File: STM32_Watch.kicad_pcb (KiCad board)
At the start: 2 copper layers, 40 x 45 mm, 44 parts, among them SW1 SW_Push, SW2 SW_Push, U1 STM32L031K6Ux, U3 LSM6DS3, X1 32.768k

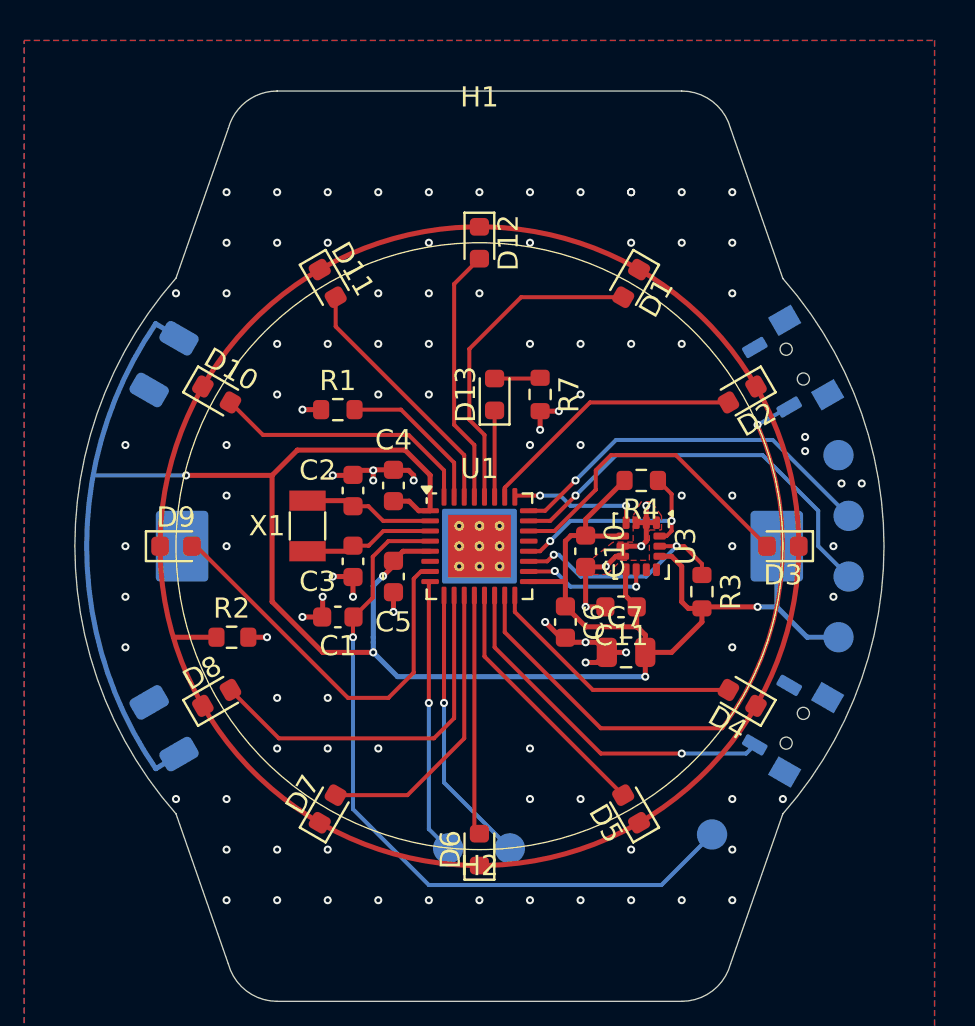
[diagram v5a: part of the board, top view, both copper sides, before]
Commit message: Updated Routing & Fixed DRC problems
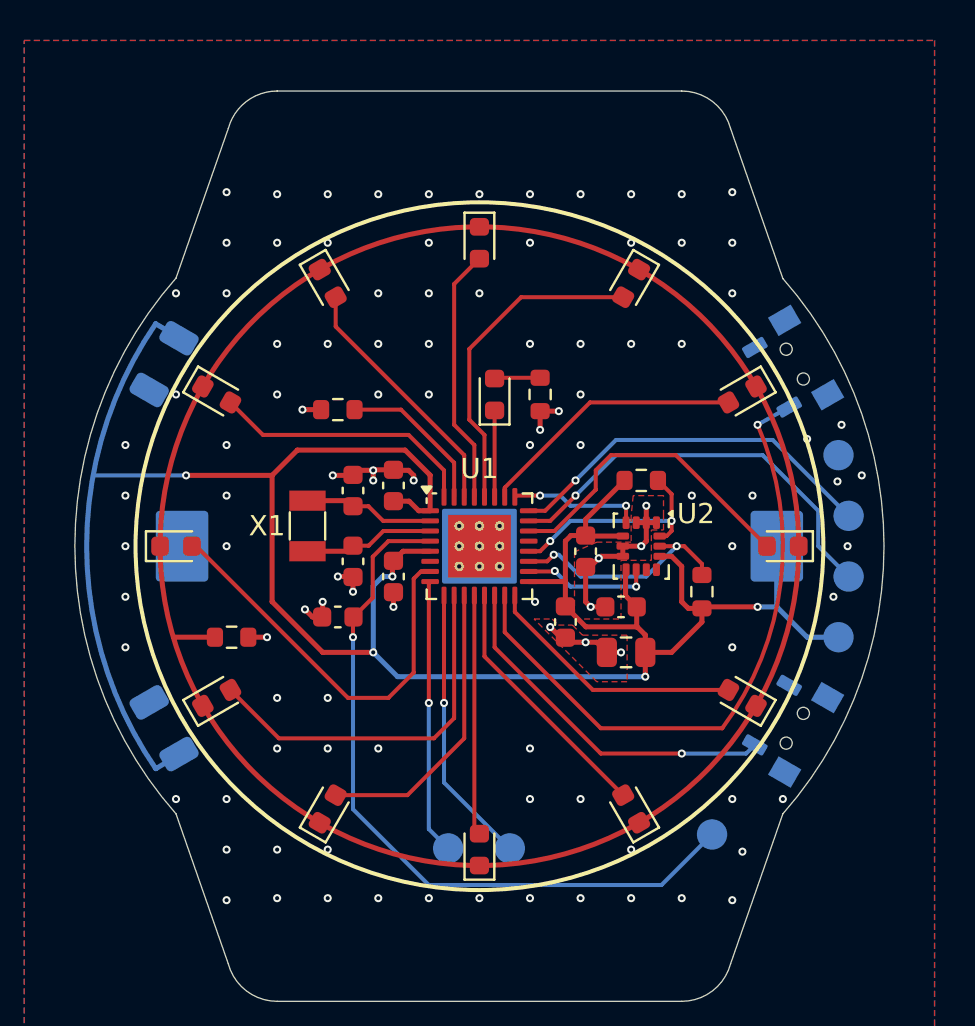
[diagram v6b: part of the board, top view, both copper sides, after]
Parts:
- removed R7: 1M, Resistor_SMD:R_0603_1608Metric
- removed U3: LSM6DS3, Package_LGA:LGA-14_3x2.5mm_P0.5mm_LayoutBorder3x4y
- added R5: 1M, Resistor_SMD:R_0603_1608Metric, F.Cu at (103.0, 92.5)
- added U2: LSM6DS3, Package_LGA:LGA-14_3x2.5mm_P0.5mm_LayoutBorder3x4y, F.Cu at (108.0, 100.0)
- turned TP5 to -90 degrees
- turned TP6 to -90 degrees
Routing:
- net GND: track 29.3 -> 26.3 mm, vias 106 -> 107
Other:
- board text added: "3V3"
- board text added: "CL"
- board text added: "GND"
- board text added: "IO"
- board text added: "NRST"
- board text added: "RX"
- board text added: "TX"

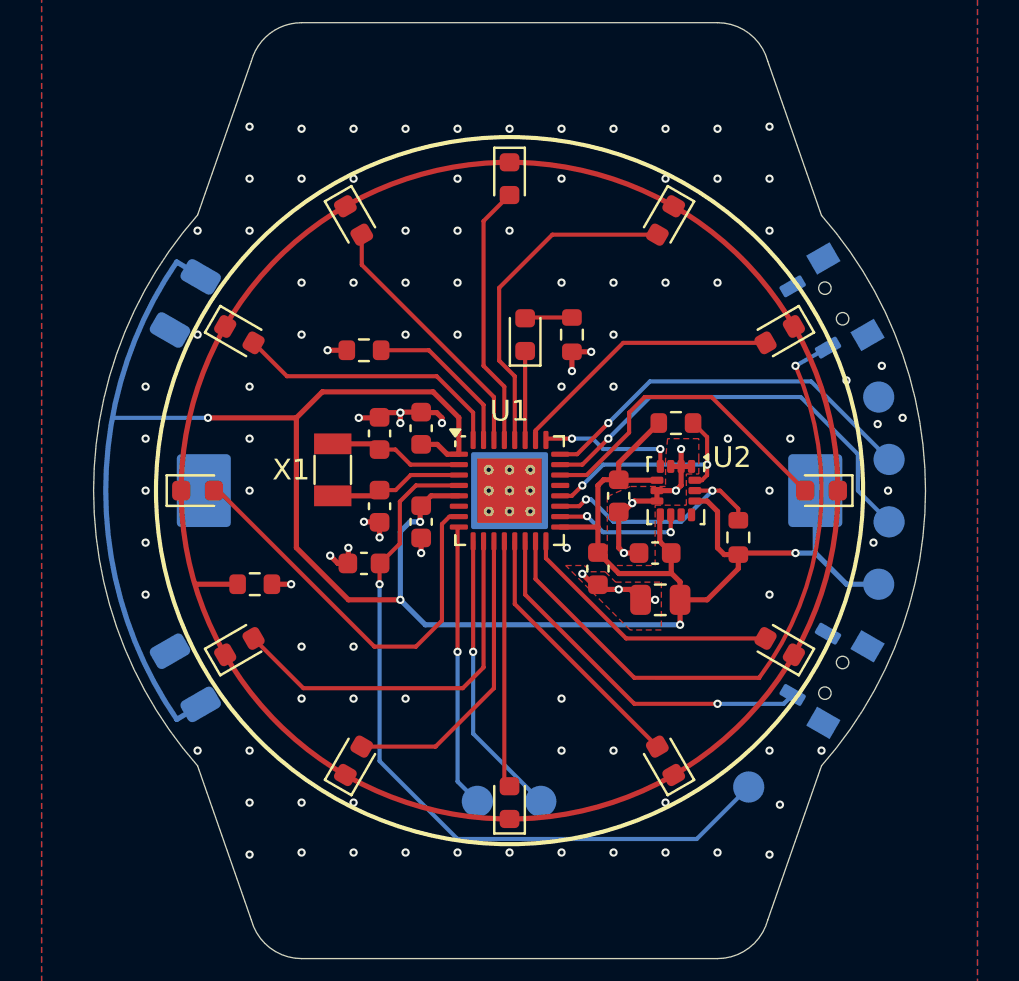
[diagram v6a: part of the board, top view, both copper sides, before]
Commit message: Added silkscreen stuff
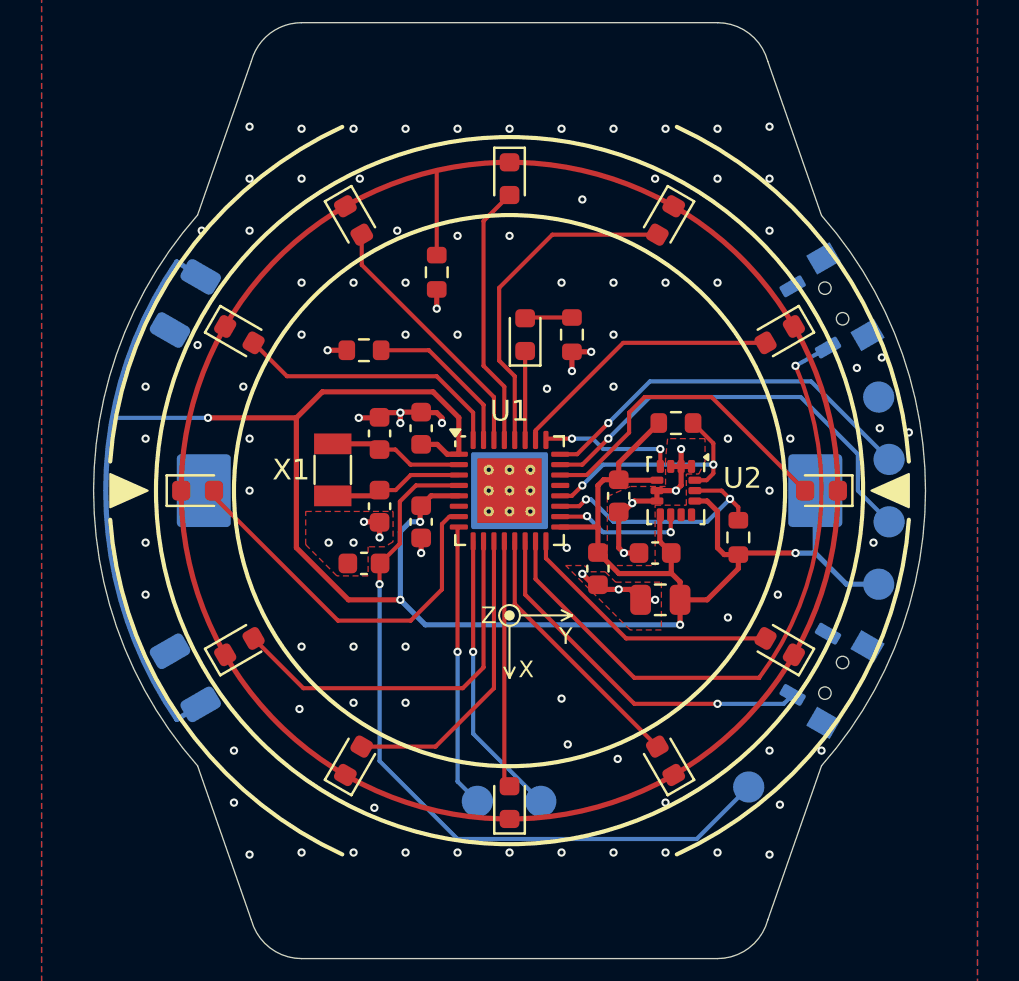
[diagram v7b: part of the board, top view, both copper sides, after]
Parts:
- moved R2 17.4 mm to (96.5, 89.5), turned to -90 degrees
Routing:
- net GND: track 26.3 -> 24.5 mm, vias 107 -> 103
- net LED_9: track 20.2 -> 18.4 mm
- net I2C_SCL: track 11.5 -> 12.2 mm
- net I2C_SDA: track 11.2 -> 11.8 mm
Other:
- board text added: "01/26 REV: A"
- board text added: "CR2032 ONLY"
- board text added: "X"
- board text added: "Y"
- board text added: "Z"

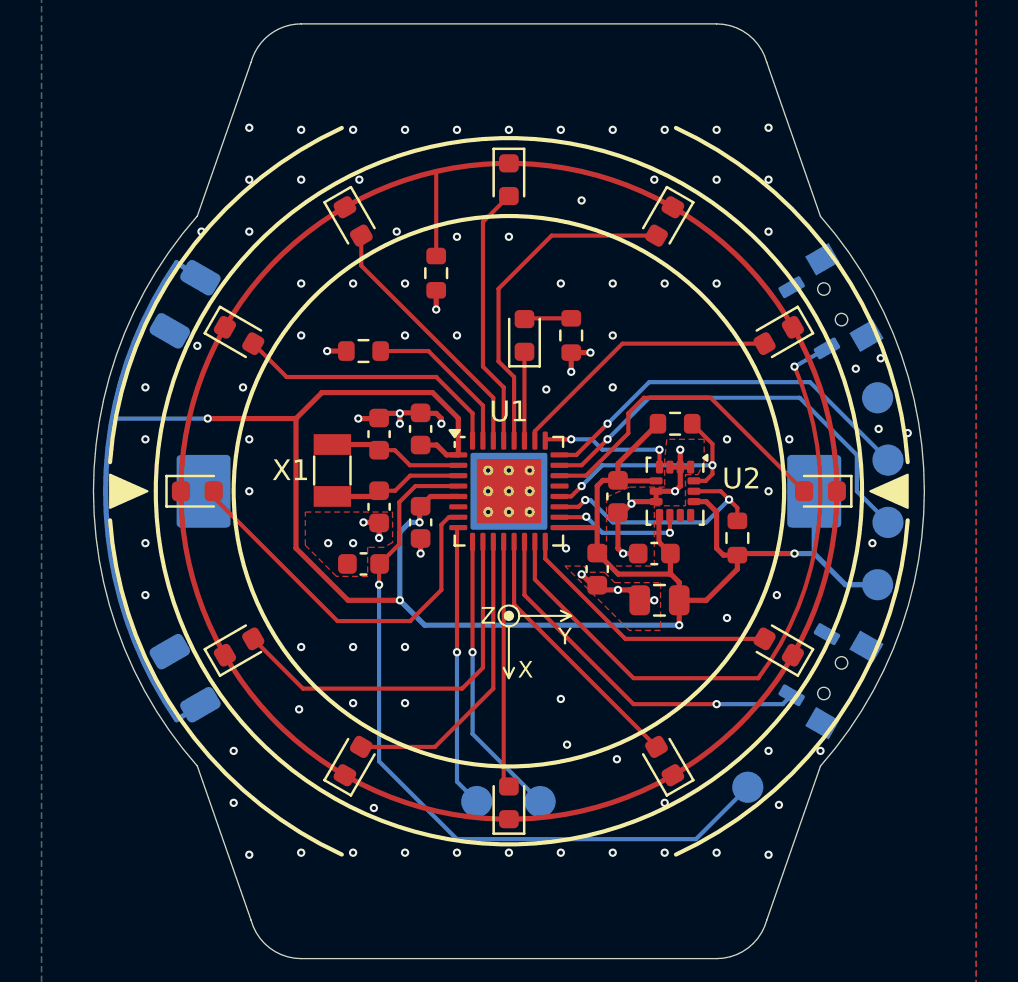
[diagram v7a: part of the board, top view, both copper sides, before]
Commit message: Rerouted 100uF caps & Via/Pad hole size 0.2->0.3
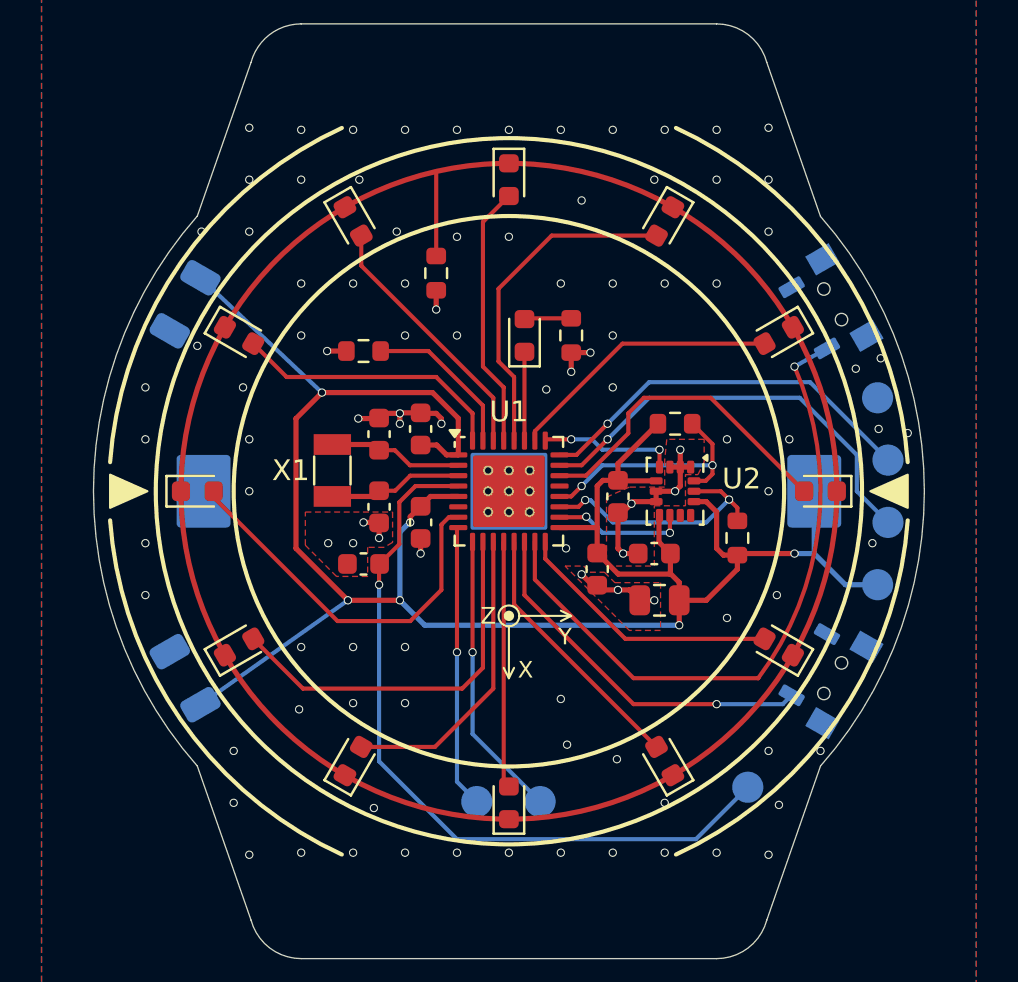
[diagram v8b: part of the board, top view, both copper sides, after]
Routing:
- net VDD: track 90.2 -> 85.8 mm, vias 5 -> 6
